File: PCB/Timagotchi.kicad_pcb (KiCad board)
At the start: 2 copper layers, 11 parts, among them J1 Conn_01x13_Pin, J2 Conn_01x02_Pin, SW1 SW_Omron_B3FS, SW2 SW_Omron_B3FS, SW3 SW_Omron_B3FS, SW4 SW_Omron_B3FS, SW5 SW_Omron_B3FS, SW6 SW_Omron_B3FS, U1 XIAO-ESP32-S3-Plus-SMD, U2 MAX98357A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

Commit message: optimizations and other stuff.
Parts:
- removed J1: Conn_01x13_Pin, Connector_JST:JST_SH_SM13B-SRSS-TB_1x13-1MP_P1.00mm_Horizontal
- removed SW5, SW6: SW_Omron_B3FS, Button_Switch_SMD:SW_SPST_Omron_B3FS-100xP
- added 1.47inch LCD Display: 1.47inch LCD Display, Library:1.47inch LCD Display, F.Cu at (80.8, 87.6)
- added J3: 2005280180, Connector_FFC-FPC:Molex_200528-0180_1x18-1MP_P1.00mm_Horizontal, F.Cu at (140.0, 83.1)
- moved SW3 141.0 mm to (196.0, 69.0)
- moved SW1 131.4 mm to (183.5, 78.5)
- moved SW4 130.3 mm to (184.0, 56.5)
- moved SW2 116.3 mm to (171.0, 67.5)
- moved U2 46.2 mm to (124.3, 64.5), turned to -90 degrees
- moved U1 42.9 mm to (136.9, 68.1), turned to 90 degrees
- moved U3 41.3 mm to (105.5, 66.0)
- moved J2 33.5 mm to (122.5, 74.0)
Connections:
- U1 pad 10: /TP_RST -> unconnected-(U1-GPIO8_A9_D9_MISO-Pad10)
- U1 pad 11: /MOSI -> /SEL
- U1 pad 14: unconnected-(U1-VBUS-Pad14) -> +5V
- U1 pad 18: /SW4 -> /LCD_CS
- U1 pad 19: /SW5 -> /HPOS
- U1 pad 2: /SD_CS -> /MOSI
- U1 pad 20: /SW6 -> /VPOS
- U1 pad 25: /SEL -> unconnected-(U1-GPIO40_MTDO_CAM_SDA_I2S_WS-Pad25)
- U1 pad 28: /HPOS -> unconnected-(U1-GPIO42_MTMS_PDM_CLK_TX1-Pad28)
- U1 pad 29: /VPOS -> unconnected-(U1-GPIO39_MTCK_CAM_SCL_I2S_SCK-Pad29)
- U1 pad 8: /LCD_CS -> /SW4
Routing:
- net /I2S_WS: track 0.00 -> 0.62 mm

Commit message: Pcb changes, mostly files and 3d models.
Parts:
- removed J2: Conn_01x02_Pin, Connector_JST:JST_PH_B2B-PH-K_1x02_P2.00mm_Vertical
- removed J3: 2005280180, Connector_FFC-FPC:Molex_200528-0180_1x18-1MP_P1.00mm_Horizontal
- removed SW4: SW_Omron_B3FS, Button_Switch_SMD:SW_SPST_Omron_B3FS-100xP
- removed U3: COM-09032, Joystick footprint:XDCR_COM-09032
- added Battery: Conn_01x02_Pin, Connector_JST:JST_PH_B2B-PH-K_1x02_P2.00mm_Vertical, F.Cu at (171.5, 61.0)
- added J1: Conn_01x04, Library:JOYSTICK-PSP1000, F.Cu at (137.5, 51.8)
- added ScreenConnector1: 2005280180, FFC:CON_2005280180_MOL, F.Cu at (154.5, 68.0)
- moved U2 48.2 mm to (171.3, 53.8), turned to 180 degrees
- moved U1 29.0 mm to (159.5, 50.0)
- moved SW3 26.8 mm to (196.0, 42.2)
- moved SW2 20.6 mm to (184.0, 51.5)
- moved SW1 20.4 mm to (195.5, 62.0)
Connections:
- U1 pad 10: unconnected-(U1-GPIO8_A9_D9_MISO-Pad10) -> /I2S_SD
- U1 pad 11: /SEL -> unconnected-(U1-GPIO9_A10_D10_MOSI-Pad11)
- U1 pad 15: /I2S_SD -> unconnected-(U1-GPIO38_DVP_VSYNC_I2S_SD-Pad15)
- U1 pad 16: /I2S_SCK -> unconnected-(U1-GPIO39_CAM_SCL_I2S_SCK-Pad16)
- U1 pad 17: /I2S_WS -> /SCLK
- U1 pad 19: /HPOS -> /VPOS
- U1 pad 20: /VPOS -> /HPOS
- U1 pad 21: /SW1 -> /SW2
- U1 pad 22: /SW2 -> /I2S_SCK
- U1 pad 8: /SW4 -> /SW1
- U1 pad 9: /SCLK -> /I2S_WS
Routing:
- net /I2S_WS: track 0.62 -> 0.00 mm

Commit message: puh cuh buh 2
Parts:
- J1: value Conn_01x04 -> Joystick
- moved 1.47inch LCD Display 82.2 mm to (149.0, 41.8)
- moved U1 24.8 mm to (184.2, 51.4)
- moved U2 24.8 mm to (196.1, 55.2)
- moved ScreenConnector 24.5 mm to (161.5, 44.5), turned to 180 degrees
- moved SW2 20.8 mm to (204.5, 54.8)
- moved Battery 17.4 mm to (187.5, 68.0)
- moved SW3 9.22 mm to (205.0, 44.2)
- moved SW1 8.93 mm to (204.0, 64.8)
- moved J1 1.75 mm to (137.5, 50.0)
- renumbered ScreenConnector1 to ScreenConnector
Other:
- board outline added: 90 x 35 mm

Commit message: PCB wiringgg
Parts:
- removed 1.47inch LCD Display: 1.47inch LCD Display, Library:1.47inch LCD Display
- added LS1: CMS-201438-058S, Speaker speaker:SPKR_CMS-201438-058S, B.Cu at (185.5, 50.5)
- J1: value Joystick -> Conn_01x04
- moved J1 14.5 mm to (152.0, 50.5)
- moved J2 12.7 mm to (196.5, 59.0)
- moved ScreenConnector1 9.52 mm to (168.1, 51.5), turned to -90 degrees
- moved SW1 7.38 mm to (207.5, 58.2)
- moved SW2 5.41 mm to (207.5, 50.2)
- moved SW3 3.05 mm to (207.5, 42.5)
- moved U2 1.64 mm to (196.7, 53.7), turned to 90 degrees
- moved U1 1.36 mm to (184.2, 50.0)
- renumbered Battery to J2, ScreenConnector to ScreenConnector1
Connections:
- ScreenConnector1 pad 15: /TP_INT -> /LCD_DC
- ScreenConnector1 pad 7: /LCD_DC -> /TP_INT
- U1 pad 1: /TP_INT -> /LCD_BL
- U1 pad 10: /I2S_SD -> /I2S_WS
- U1 pad 17: /SCLK -> /TP_INT
- U1 pad 19: /VPOS -> /HPOS
- U1 pad 2: /MOSI -> /SCLK
- U1 pad 20: /HPOS -> /TP_SDA
- U1 pad 3: /LCD_BL -> /MOSI
- U1 pad 5: /TP_SDA -> /VPOS
- U1 pad 9: /I2S_WS -> /I2S_SD
- U2 pad 10: unconnected-(U2-OUTN-Pad10) -> Net-(U2-OUTN)
- U2 pad 9: unconnected-(U2-OUTP-Pad9) -> Net-(U2-OUTP)
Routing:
- net GND: track 0.00 -> 91.9 mm, vias 0 -> 10
- net /SW3: track 0.00 -> 23.7 mm
- net /SW2: track 0.00 -> 23.0 mm, vias 0 -> 2
- net /SW1: track 0.00 -> 19.7 mm
- net /VPOS: track 0.00 -> 17.5 mm
- net /HPOS: track 0.00 -> 16.0 mm
- net /VBAT: track 0.00 -> 15.4 mm
- net +3.3V: track 0.00 -> 13.7 mm, vias 0 -> 2
- net Net-(U2-OUTP): track 0.00 -> 8.39 mm, vias 0 -> 1
- net Net-(U2-OUTN): track 0.00 -> 7.14 mm, vias 0 -> 1
- net /LCD_BL: track 0.00 -> 6.14 mm
- net /SCLK: track 0.00 -> 5.92 mm
- net /LCD_DC: track 0.00 -> 5.74 mm
- net /MOSI: track 0.00 -> 5.67 mm
- net /TP_SCL: track 0.00 -> 5.51 mm
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- added copper zone on F.Cu, net +3.3V
- added copper zone on B.Cu, net GND
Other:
- board size 90 x 35 mm -> 75 x 27 mm

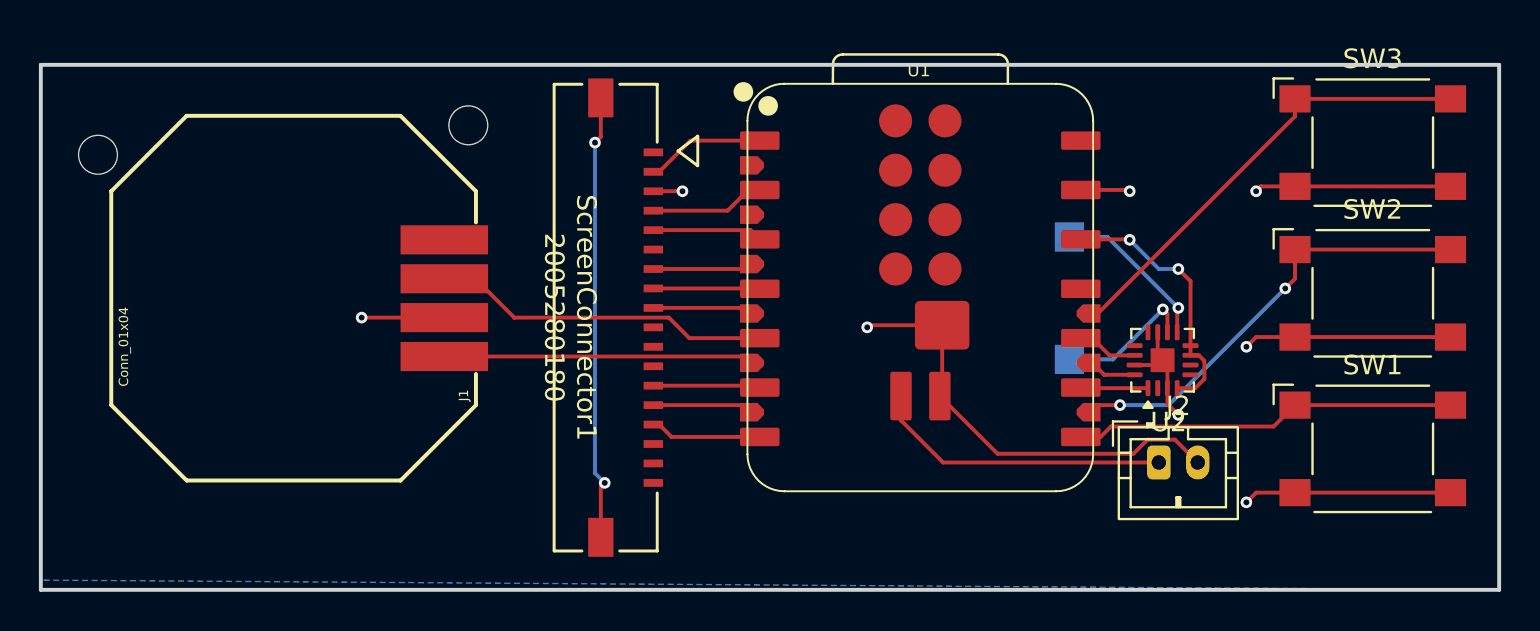
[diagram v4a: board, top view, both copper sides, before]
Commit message: moved the battery connector to the back
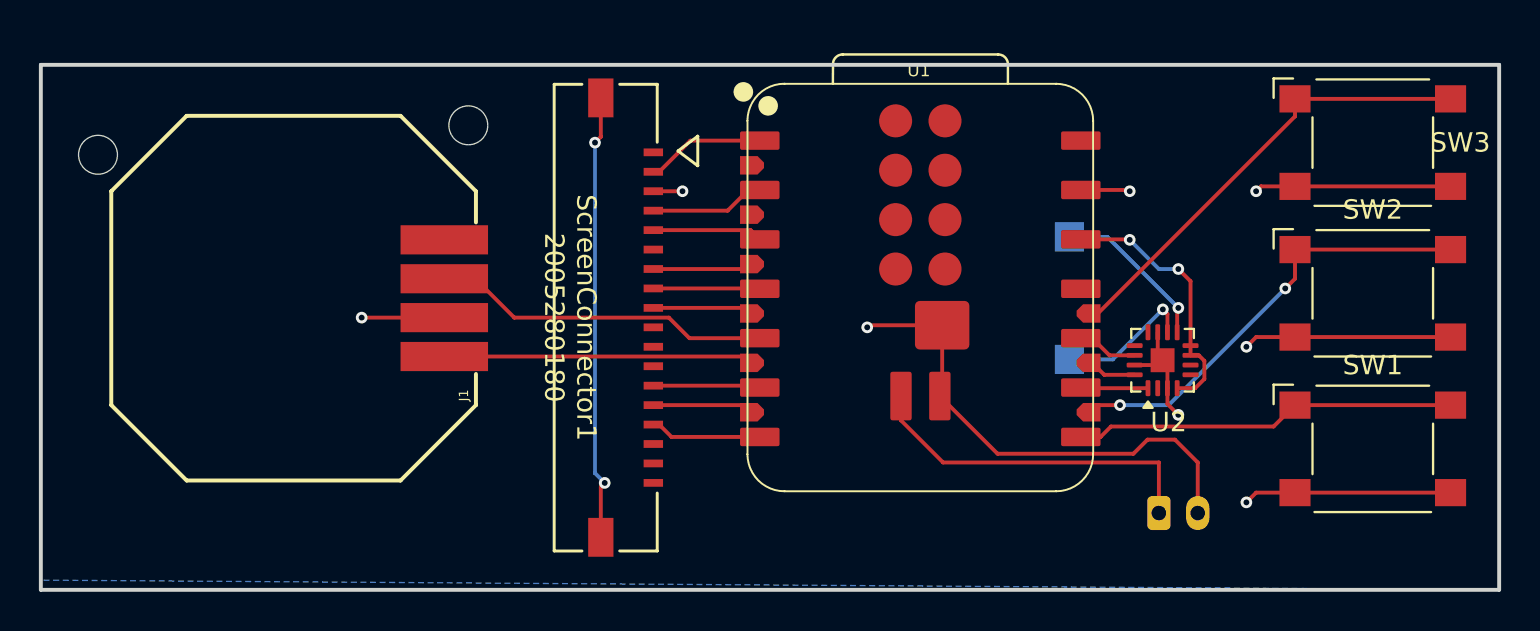
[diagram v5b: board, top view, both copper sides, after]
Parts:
- J2: moved to B.Cu
- moved J2 2.60 mm to (196.5, 61.5)
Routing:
- net GND: track 91.9 -> 94.5 mm
- net /VBAT: track 15.4 -> 18.0 mm
